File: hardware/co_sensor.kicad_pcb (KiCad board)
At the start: 2 copper layers, 43.2 x 84.5 mm, 16 parts, among them P1 CONN28, P2 CONN28, P3 CONN6, U1 110-109, U2 AD8603

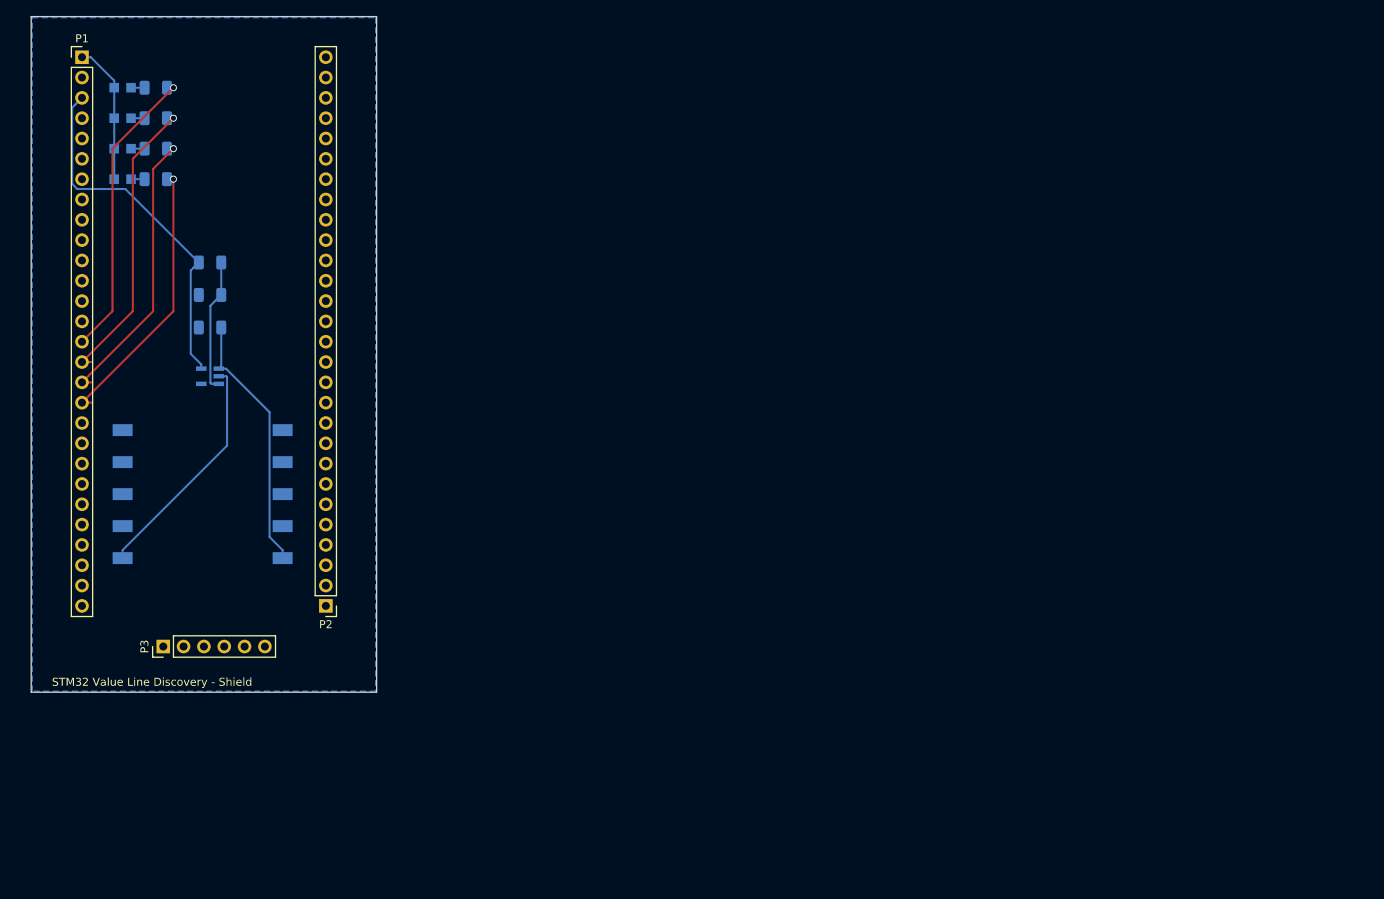
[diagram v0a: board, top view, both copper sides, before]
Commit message: Completely refactors the board with a new sensor and processor. Adds a .gitignore
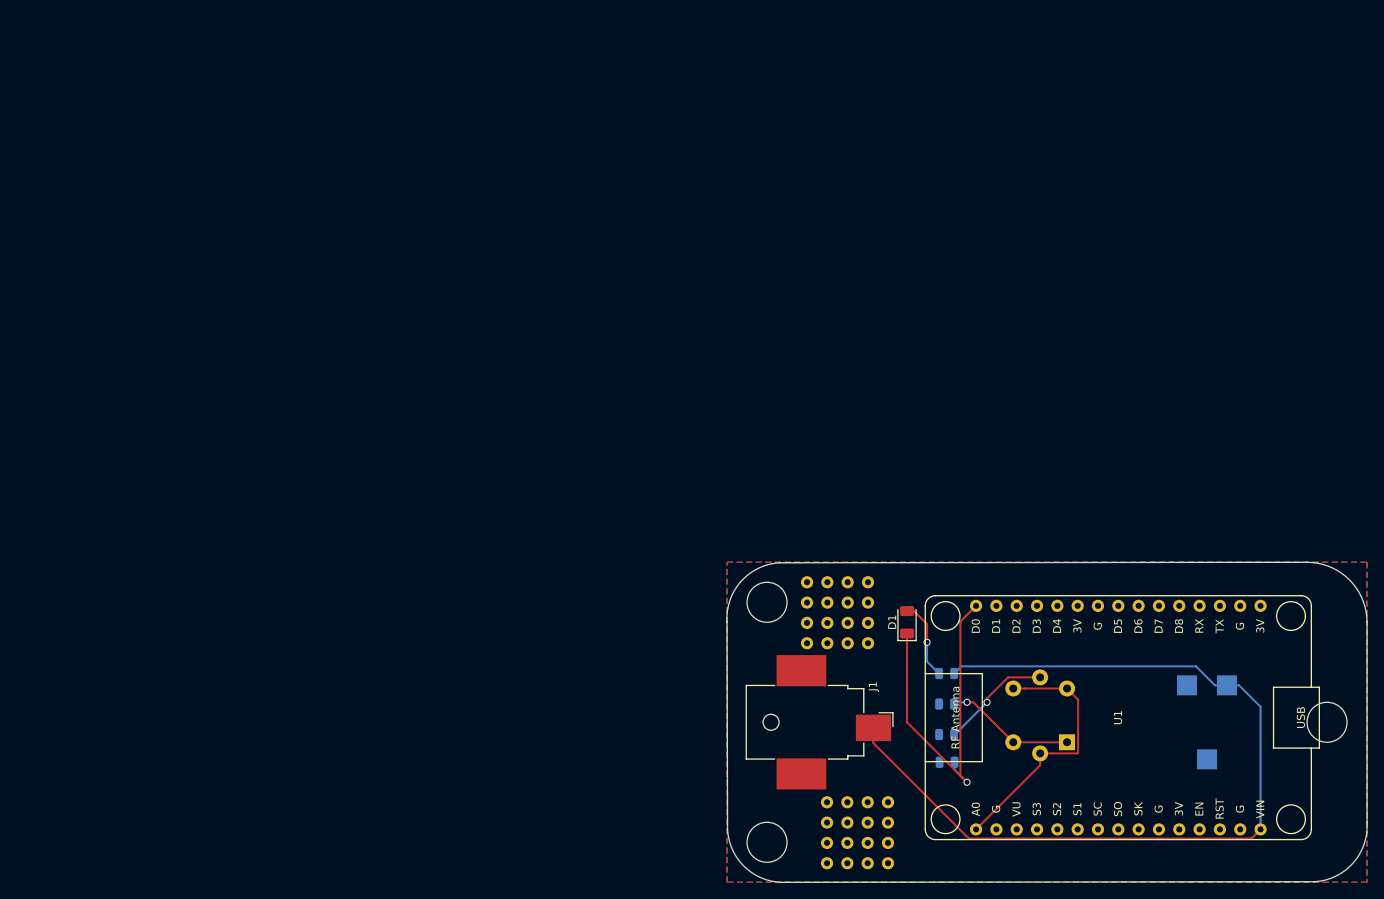
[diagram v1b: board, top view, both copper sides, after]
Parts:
- removed D2, D3, D4: LTST-C171KGKT, digikey-footprints:0805
- removed P1, P2: CONN28, Connector_PinHeader_2.54mm:PinHeader_1x28_P2.54mm_Vertical
- removed P3: CONN6, Connector_PinHeader_2.54mm:PinHeader_1x06_P2.54mm_Vertical
- removed R4: 40ohm, SMD_Resistor_Footprints:R_1206_3216Metric
- removed R5, R6: R, smd_resistors:R_1206_3216Metric
- added J1: Barrel_Jack, Connector_BarrelJack:BarrelJack_CUI_PJ-036AH-SMT_Horizontal, F.Cu at (132.5, 122.5)
- added REF**: VIA-0.6mm, VIA-0.6mm, F.Cu at (132.5, 110.1)
- added REF**: VIA-0.6mm, VIA-0.6mm, F.Cu at (132.5, 112.6)
- added REF**: VIA-0.6mm, VIA-0.6mm, F.Cu at (135.1, 110.1)
- added REF**: VIA-0.6mm, VIA-0.6mm, F.Cu at (135.1, 105.0)
- added REF**: VIA-0.6mm, VIA-0.6mm, F.Cu at (137.6, 107.5)
- added REF**: VIA-0.6mm, VIA-0.6mm, F.Cu at (130.0, 112.6)
- added REF**: VIA-0.6mm, VIA-0.6mm, F.Cu at (132.5, 105.0)
- added REF**: VIA-0.6mm, VIA-0.6mm, F.Cu at (130.0, 110.1)
- added REF**: VIA-0.6mm, VIA-0.6mm, F.Cu at (140.1, 140.1)
- added REF**: VIA-0.6mm, VIA-0.6mm, F.Cu at (137.6, 140.1)
- added REF**: VIA-0.6mm, VIA-0.6mm, F.Cu at (135.0, 140.1)
- added REF**: VIA-0.6mm, VIA-0.6mm, F.Cu at (135.1, 112.6)
- added REF**: VIA-0.6mm, VIA-0.6mm, F.Cu at (132.5, 140.1)
- added REF**: VIA-0.6mm, VIA-0.6mm, F.Cu at (140.1, 137.6)
- added REF**: VIA-0.6mm, VIA-0.6mm, F.Cu at (137.6, 137.6)
- added REF**: VIA-0.6mm, VIA-0.6mm, F.Cu at (135.0, 137.6)
- added REF**: VIA-0.6mm, VIA-0.6mm, F.Cu at (132.5, 137.6)
- added REF**: VIA-0.6mm, VIA-0.6mm, F.Cu at (140.1, 135.0)
- added REF**: VIA-0.6mm, VIA-0.6mm, F.Cu at (137.6, 135.0)
- added REF**: VIA-0.6mm, VIA-0.6mm, F.Cu at (135.0, 135.0)
- added REF**: VIA-0.6mm, VIA-0.6mm, F.Cu at (132.5, 135.0)
- added REF**: VIA-0.6mm, VIA-0.6mm, F.Cu at (140.1, 132.5)
- added REF**: VIA-0.6mm, VIA-0.6mm, F.Cu at (137.6, 105.0)
- added REF**: VIA-0.6mm, VIA-0.6mm, F.Cu at (137.6, 132.5)
- added REF**: VIA-0.6mm, VIA-0.6mm, F.Cu at (135.0, 132.5)
- added REF**: VIA-0.6mm, VIA-0.6mm, F.Cu at (132.5, 132.5)
- added REF**: VIA-0.6mm, VIA-0.6mm, F.Cu at (137.6, 110.1)
- added REF**: VIA-0.6mm, VIA-0.6mm, F.Cu at (130.0, 107.5)
- added REF**: VIA-0.6mm, VIA-0.6mm, F.Cu at (130.0, 105.0)
- added REF**: VIA-0.6mm, VIA-0.6mm, F.Cu at (137.6, 112.6)
- added REF**: VIA-0.6mm, VIA-0.6mm, F.Cu at (132.5, 107.5)
- added REF**: VIA-0.6mm, VIA-0.6mm, F.Cu at (135.1, 107.5)
- added RV1: R_POT, Potentiometer_SMD:Potentiometer_ACP_CA9-VSMD_Vertical, B.Cu at (180.0, 122.5)
- C1: value 0.1 uF -> C; footprint smd_capacitor:C_1206_3216Metric -> Capacitor_SMD:C_0805_2012Metric
- D1: value LTST-C171KRKT -> LED; footprint digikey-footprints:0805 -> Diode_SMD:D_1206_3216Metric; moved to F.Cu
- R1, R2, R3: value 40ohm -> R; footprint SMD_Resistor_Footprints:R_1206_3216Metric -> Resistor_SMD:R_0805_2012Metric
- U1: value 110-109 -> NodeMCU1.0(ESP-12E); footprint digikey-footprints:Gas_Sensor_110-109 -> ESP8266:NodeMCU1.0(12-E); moved to F.Cu
- U2: value AD8603 -> MQ-7; footprint footprints:AD8603AUJZ-R2 -> Sensor:MQ-6
- moved R1 127.7 mm to (147.4, 124.0)
- moved R2 123.0 mm to (147.4, 120.2)
- moved D1 118.7 mm to (142.5, 110.0), turned to 90 degrees
- moved R3 118.6 mm to (147.4, 116.4)
- moved U1 117.8 mm to (168.9, 121.9), turned to 90 degrees
- moved U2 116.5 mm to (162.5, 125.0), turned to 90 degrees
- moved C1 107.0 mm to (147.5, 127.5)
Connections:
- C1 pad 1: Net-(C1-Pad1) -> DOUT
- C1 pad 2: Net-(C1-Pad2) -> GND
- D1 pad 1: Net-(D1-Pad1) -> DOUT
- D1 pad 2: GND -> Net-(D1-Pad2)
- R1 pad 1: /PA0 -> Net-(R1-Pad1)
- R1 pad 2: Net-(D1-Pad1) -> GND
- R2 pad 1: /PA1 -> Net-(R2-Pad1)
- R2 pad 2: Net-(D2-Pad1) -> GND
- R3 pad 1: /PA2 -> VCC
- R3 pad 2: Net-(D3-Pad1) -> Net-(D1-Pad2)
- U1 pad 1: Net-(U1-Pad1) -> AOUT
- U1 pad 10: Net-(U1-Pad10) -> GND
- U1 pad 6: Net-(C1-Pad1) -> Net-(U1-Pad6)
- U2 pad 1: Net-(C1-Pad1) -> Net-(R2-Pad1)
- U2 pad 2: Net-(U1-Pad5) -> AOUT
- U2 pad 3: Net-(R5-Pad1) -> Net-(R2-Pad1)
- U2 pad 4: GND -> AOUT
- U2 pad 5: +3V3 -> Net-(R1-Pad1)
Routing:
- net VCC: track 0.00 -> 111.8 mm
- net DOUT: track 0.00 -> 48.1 mm, vias 0 -> 1
- net +3V3: track 45.4 -> 0.00 mm
- net /PA0: track 37.8 -> 0.00 mm, vias 1 -> 0
- net /PA1: track 37.7 -> 0.00 mm, vias 1 -> 0
- net /PA2: track 36.4 -> 0.00 mm, vias 1 -> 0
- net /PA3: track 35.1 -> 0.00 mm, vias 1 -> 0
- net AOUT: track 0.00 -> 32.9 mm
- net Net-(C1-Pad1): track 32.8 -> 0.00 mm
- net Net-(U1-Pad5): track 29.1 -> 0.00 mm
- net GND: track 17.6 -> 0.00 mm
- net Net-(R5-Pad1): track 16.7 -> 0.00 mm
- net Net-(R2-Pad1): track 0.00 -> 16.3 mm, vias 0 -> 1
- net Net-(R1-Pad1): track 0.00 -> 14.0 mm, vias 0 -> 1
- net Net-(D1-Pad2): track 0.00 -> 9.98 mm, vias 0 -> 1
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- added copper zone on F.Cu, net GND
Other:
- board size 43.2 x 84.5 mm -> 80 x 40 mm
- board text removed: "Alert"
- board text removed: "Boot"
- board text removed: "Conn"
- board text removed: "STM32 Value Line Discovery - Shield"
- board text removed: "Stat"

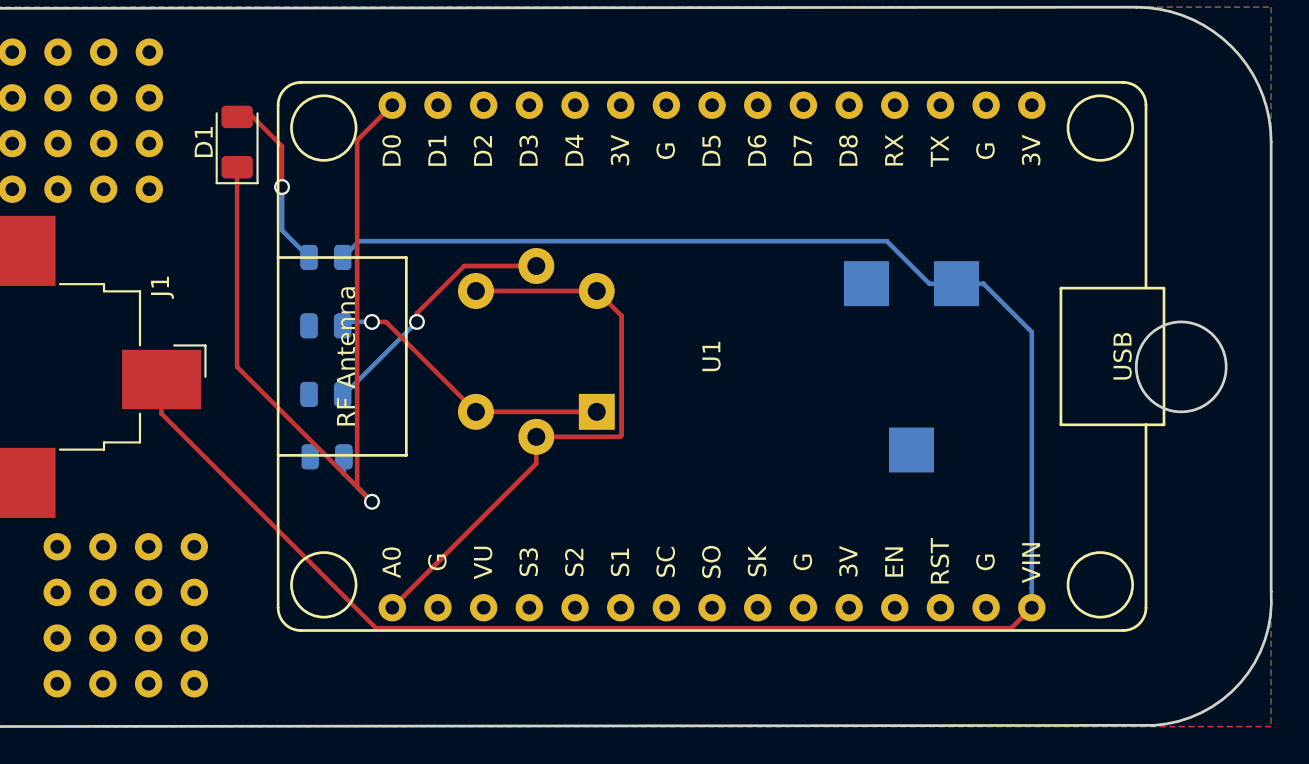
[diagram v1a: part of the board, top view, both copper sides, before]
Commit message: Updates with new LM393AR footprint and schematic item
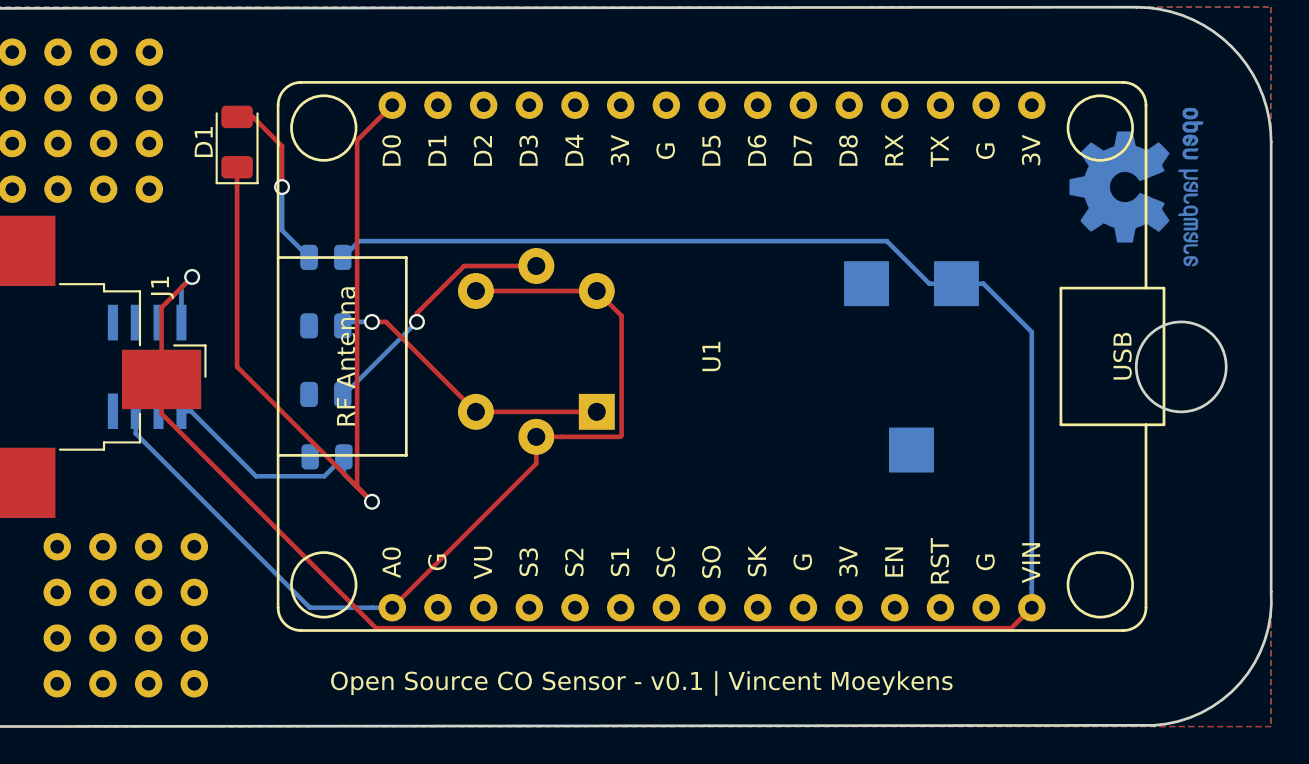
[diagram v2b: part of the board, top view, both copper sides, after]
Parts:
- added REF**: OSHW-Logo2_9.8x8mm_Copper, Symbol:OSHW-Logo2_9.8x8mm_Copper, B.Cu at (192.5, 112.5)
- added U3: LM393ADR, LM393AR:LM393ADR, B.Cu at (137.5, 122.5)
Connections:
- net DOUT renamed COMPOUT
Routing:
- net AOUT: track 32.9 -> 52.4 mm
- net COMPOUT: track 48.1 -> 59.0 mm
- net VCC: track 111.8 -> 121.0 mm, vias 0 -> 1
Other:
- board text added: "Open Source CO Sensor - v0.1 | Vincent Moeykens"
